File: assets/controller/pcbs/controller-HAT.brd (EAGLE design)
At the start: 53.3 x 22.9 mm, 12 parts

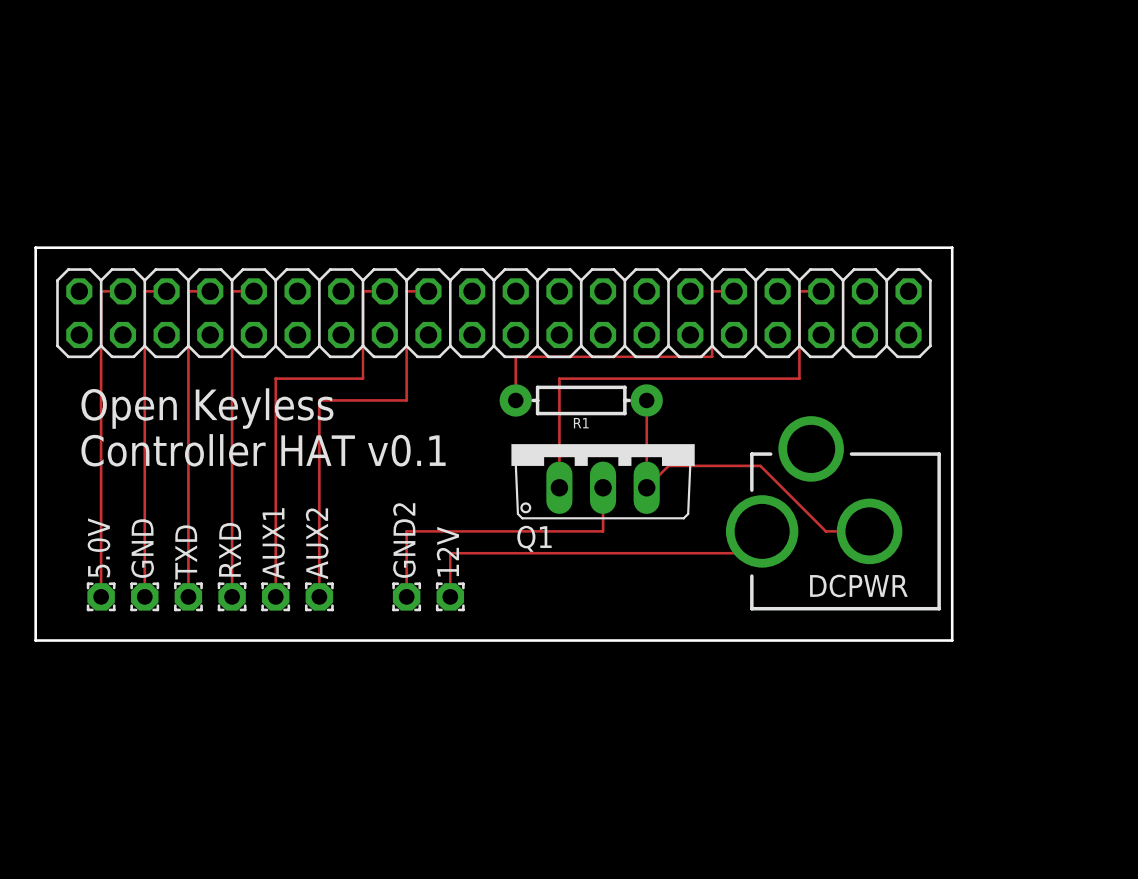
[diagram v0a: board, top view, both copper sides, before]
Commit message: Updated the controller hat.
This commit updates the controller hat to include a voltage regulator. This will
allow a single, 12v power source to power both the strike and the raspberry pi
through the 5v pin.
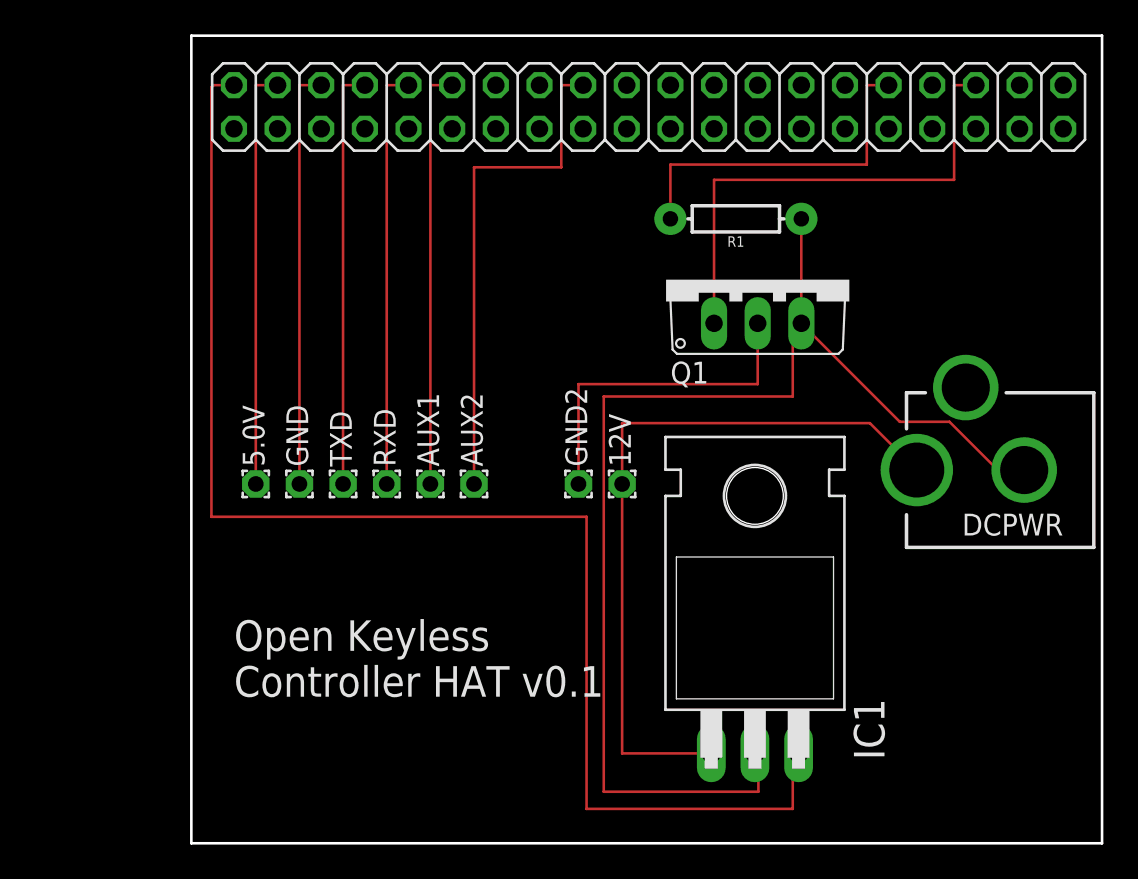
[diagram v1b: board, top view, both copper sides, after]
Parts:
- added IC1: 7805T, adafruit:TO220H
- moved GPIO 15.0 mm to (63.6, 81.8)
- moved R1 13.9 mm to (68.7, 75.3)
- moved Q1 13.1 mm to (70.0, 71.8)
- moved 12V 12.0 mm to (62.1, 59.9)
- moved GND2 12.0 mm to (59.5, 59.9)
- moved 5.0V 11.1 mm to (40.8, 59.9)
- moved AUX1 11.1 mm to (50.9, 59.9)
- moved AUX2 11.1 mm to (53.5, 59.9)
- moved GND 11.1 mm to (43.3, 59.9)
- moved RXD 11.1 mm to (48.4, 59.9)
- moved TXD 11.1 mm to (45.8, 59.9)
- moved DCPWR 9.68 mm to (92.8, 60.7)
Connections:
- new net N$12: GPIO.2, IC1.3
- net N$10: now also GPIO.12; no longer GPIO.16
- net N$2: now also IC1.1
- net N$4: now also IC1.2
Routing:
- net N$12: track 0.00 -> 80.6 mm
- net N$4: track 20.2 -> 72.4 mm
- net N$2: track 22.0 -> 42.7 mm
- net N$9: track 19.1 -> 24.5 mm
- net N$8: track 19.1 -> 24.5 mm
- net N$7: track 19.1 -> 24.5 mm
- net N$6: track 19.1 -> 24.5 mm
- net N$11: track 24.1 -> 29.6 mm
- net N$5: track 26.7 -> 29.1 mm
- net N$1: track 17.8 -> 19.8 mm
- net N$3: track 19.1 -> 20.5 mm
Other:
- board size 53.3 x 22.9 mm -> 53 x 47 mm
